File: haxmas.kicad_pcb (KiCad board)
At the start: 2 copper layers, 33 x 32 mm, 23 parts, among them J1 edge +, J2 b-, J3 edge -, J4 b+, J5 edge +, J6 edge -

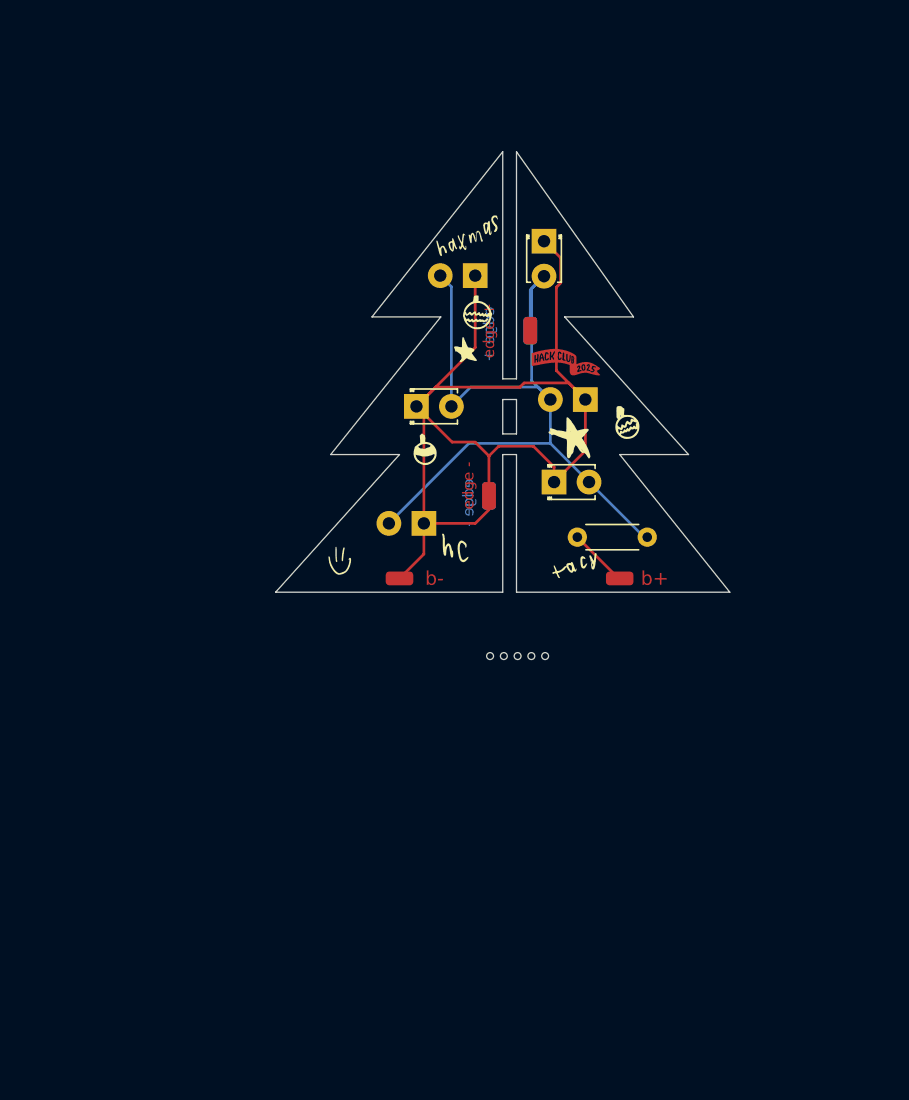
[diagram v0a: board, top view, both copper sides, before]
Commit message: feat: add large version
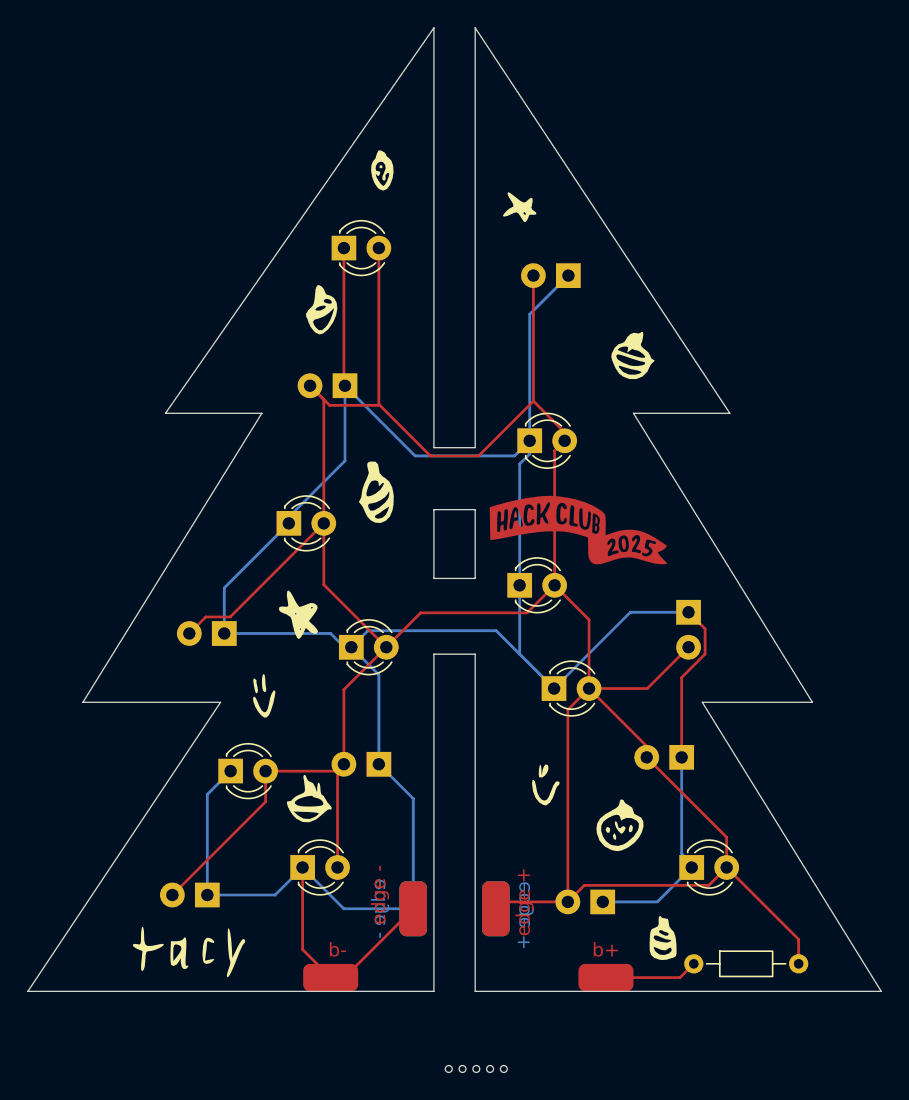
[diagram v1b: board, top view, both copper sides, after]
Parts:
- removed the G*** at (107.1, 54.3) (x2)
- removed the G*** at (102.5, 55.0)
- removed the G*** at (104.2, 55.5)
- removed the G*** at (98.5, 69.0)
- added D10: LED, LED_THT:LED_D3.0mm, F.Cu at (106.2, 78.0)
- added D11: LED, LED_THT:LED_D3.0mm, B.Cu at (107.3, 48.0)
- added D12: LED, LED_THT:LED_D3.0mm, F.Cu at (91.0, 46.0)
- added D13: LED, LED_THT:LED_D3.0mm, F.Cu at (82.7, 84.0)
- added D14: LED, LED_THT:LED_D3.0mm, B.Cu at (93.5, 83.5)
- added D15: LED, LED_THT:LED_D3.0mm, F.Cu at (87.0, 66.0)
- added D16: LED, LED_THT:LED_D3.0mm, F.Cu at (91.5, 75.0)
- added D17: LED, LED_THT:LED_D3.0mm, B.Cu at (82.3, 74.0)
- added D7: LED, LED_THT:LED_D3.0mm, F.Cu at (104.5, 60.0)
- added D8: LED, LED_THT:LED_D3.0mm, F.Cu at (103.7, 70.5)
- added D9: LED, LED_THT:LED_D3.0mm, B.Cu at (115.5, 83.0)
- added G*** (x2): LOGO, LOGO, F.Cu at (108.0, 66.5)
- added G***: LOGO, LOGO, F.Cu at (98.0, 46.5)
- added G***: LOGO, LOGO, B.Cu at (99.5, 67.5)
- D1, D6: footprint LED_THT:LED_D1.8mm_W3.3mm_H2.4mm -> LED_THT:LED_D3.0mm; moved to B.Cu
- D2, D3, D5: footprint LED_THT:LED_D1.8mm_W3.3mm_H2.4mm -> LED_THT:LED_D3.0mm
- D4: footprint LED_THT:LED_D1.8mm_W3.3mm_H2.4mm -> LED_THT:LED_D3.0mm; moved to F.Cu
- J1, J2, J3, J4, J5, J6: footprint Connector_Wire:SolderWirePad_1x01_SMD_1x2mm -> Connector_Wire:SolderWirePad_1x01_SMD_2x4mm
- R1: footprint Resistor_THT:R_Axial_DIN0204_L3.6mm_D1.6mm_P5.08mm_Horizontal -> Resistor_THT:R_Axial_DIN0204_L3.6mm_D1.6mm_P7.62mm_Horizontal
- moved J1 42.1 mm to (102.0, 94.0)
- moved J5 42.1 mm to (102.0, 94.0)
- moved D4 34.9 mm to (116.2, 91.0), turned to 0 degrees
- moved D3 34.5 mm to (88.0, 91.0)
- moved R1 32.1 mm to (116.4, 98.0)
- moved D2 31.2 mm to (81.0, 93.0)
- moved D1 30.7 mm to (109.8, 93.5), turned to 180 degrees
- moved J3 30.5 mm to (96.0, 94.0)
- moved J6 30.5 mm to (96.0, 94.0)
- moved KiKit_MB_4_1 30.1 mm to (98.6, 105.6)
- moved KiKit_MB_4_2 30.1 mm to (99.6, 105.6)
- moved KiKit_MB_4_3 30.1 mm to (100.6, 105.6)
- moved KiKit_MB_4_4 30.1 mm to (101.6, 105.6)
- moved KiKit_MB_4_5 30.1 mm to (102.6, 105.6)
- moved J2 29.4 mm to (90.0, 99.0)
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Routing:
- net +3.3V: track 59.4 -> 216.3 mm
- net GND: track 80.7 -> 210.9 mm
- net Net-(J4-Pin_1): track 4.32 -> 6.79 mm
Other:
- board size 33 x 32 mm -> 62 x 70 mm
